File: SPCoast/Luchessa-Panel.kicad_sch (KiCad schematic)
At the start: 21 parts, among them SW8784 783, SW8796 795, SW8800 799, U8004 0x24, U8005 0x25, U8006 0x26

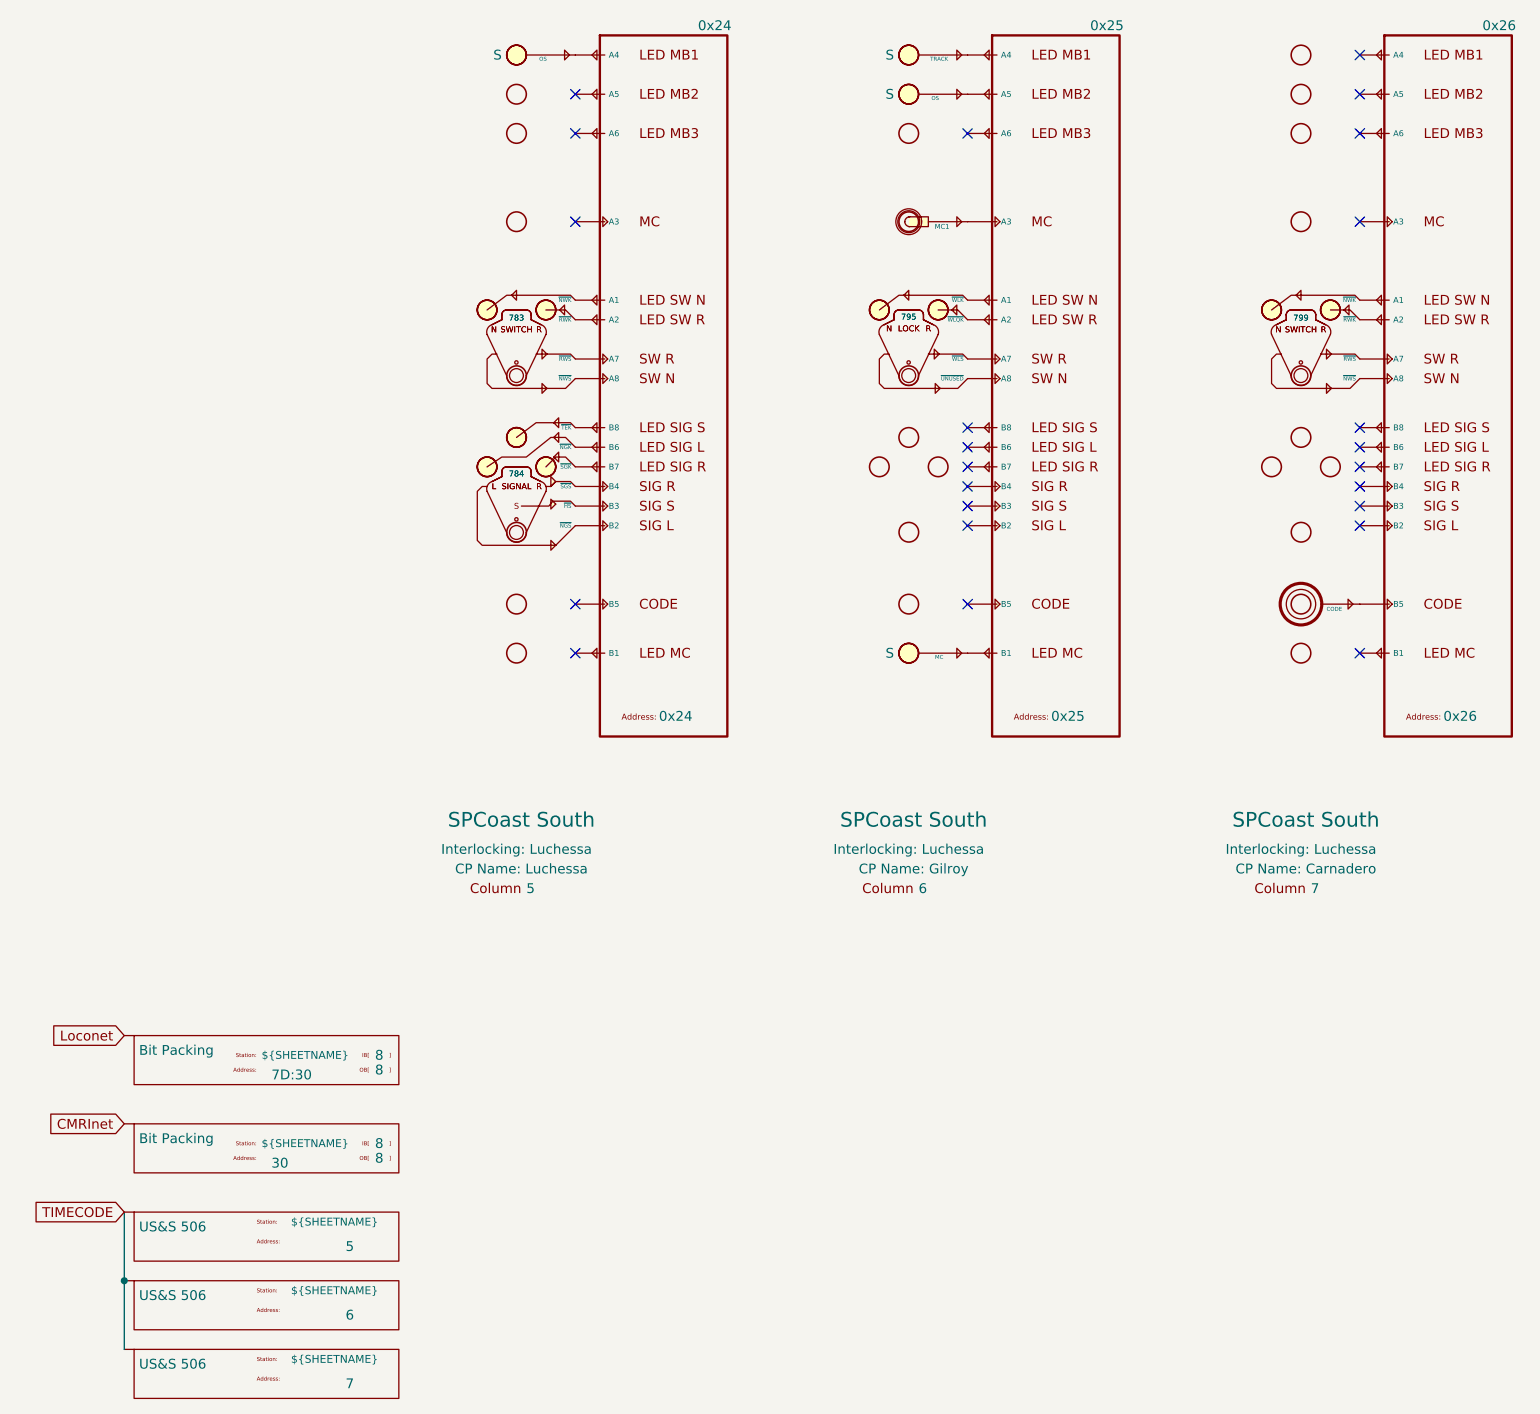
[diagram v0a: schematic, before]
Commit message: refactor(kicad): mast anchors with explicit indication-to-aspect casts; restore fields KiCad reset
Second pass after the cast chains (b4c58d3), decided 2026-10-17: the per-head
anchors Head-CPL/CL/Semaphore were the mast's indication table collapsed into
a symbol. The chain is now

    [Mast 774NAB] -indication- [Cast-Aspect-CPL unit B] -aspect- [Cast-Encoder-CPL] -bits- [chip]

Cast-Aspect-CPL/CL/Semaphore are multi-unit casts, one unit per head letter
(A..E), so placing unit B beside mast 774N is head 774NB with nothing typed;
the reader derives every head name from mast plus unit. Style's home is the
aspect cast. The project ERC now ignores missing_unit and missing_input_pin,
since an aspect cast places only the units its mast has.

CMRI bits: Address is the node (the chip every bit folds into, as for every
other driver), Bit is the bit, UA = ${Address} is a display echo, Value =
UA${Address}.IN.${Bit}.

Restore (SPCoast/edits/2026-10-17-restore-reset-fields.py): the owner's last
KiCad save before 857cae2 ran "update symbols from library" with field reset,
putting library defaults into per-instance fields on nine sheets: every
PanelLamp IndicationToken ("S"), PanelColumn Interlocking ("Luchessa"),
Luchessa encoding Station ("Panel"), Sargent Exp2 PCA9685-PWM 0x27 -> 0x20
(colliding with Exp3), and the 34 Caltrain bit numbers. All 98 values are
restored from the last good netlist export, embedded in the script.

Scripts: SPCoast/edits/2026-10-17-mast-chain.py (second pass; reuses the
first pass's helpers), 2026-10-17-restore-reset-fields.py. __pycache__/
added to .gitignore.

Verified:
- post-restore netlist vs the last good export: no field differs except on
  the anchors the first pass replaced and the intended JMRI blanks
- lint_symbol_fields: 93 symbols, 0 errors (per-unit cast rule)
- kicad-cli ERC: 0 violations; netlist export without warnings
- gate vs post-restore: nets not touching an anchor identical; all 11 aspect
  nets re-sourced from a Cast-Aspect un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
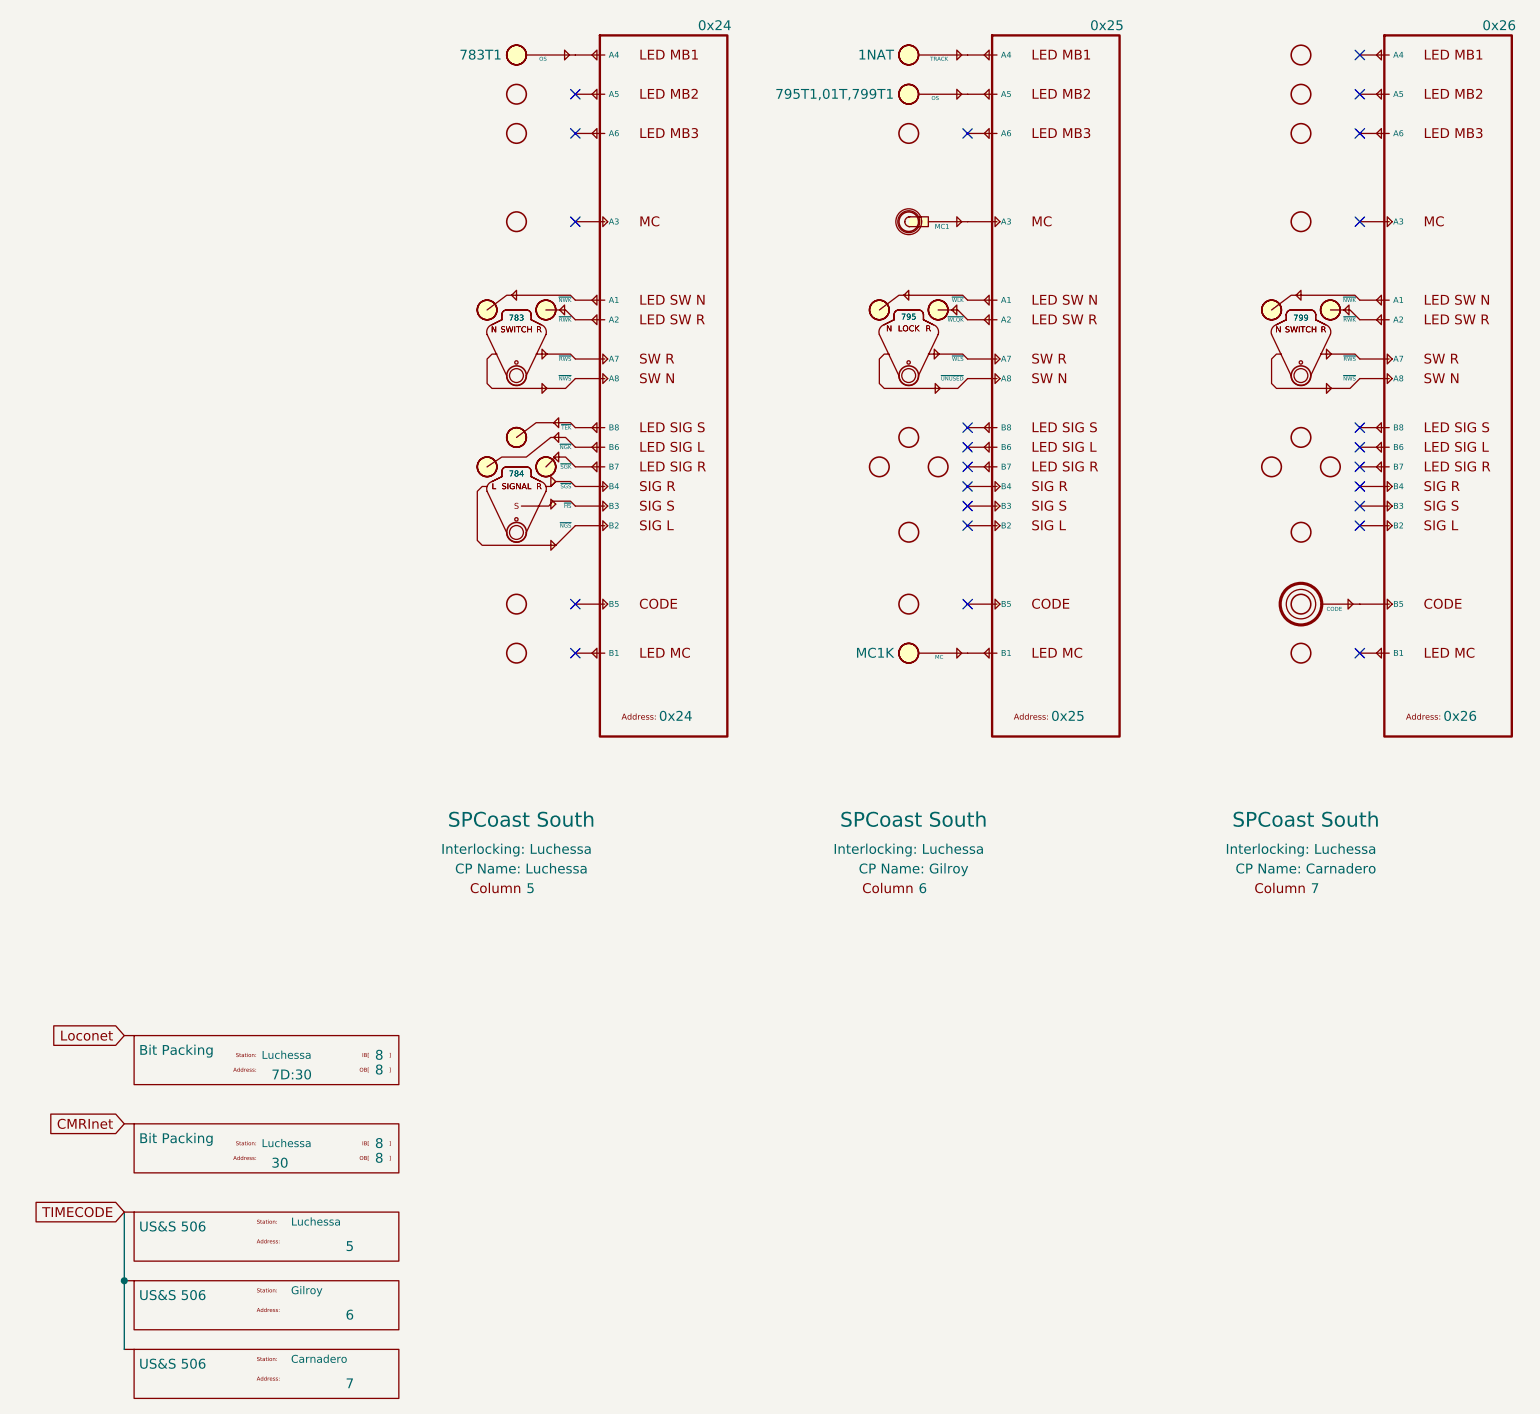
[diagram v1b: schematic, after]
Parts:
- Encoding8002, Encoding8005, Encoding8006: Station ${SHEETNAME} -> Luchessa
- Encoding8003: Station ${SHEETNAME} -> Gilroy
- Encoding8004: Station ${SHEETNAME} -> Carnadero
- LAMP8005: IndicationToken S -> 783T1
- LAMP8006: IndicationToken S -> 1NAT
- LAMP8007: IndicationToken S -> 795T1,01T,799T1
- LAMP8008: IndicationToken S -> MC1K
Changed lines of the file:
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@@
 			)
 		)
-		(property "Station" "${SHEETNAME}"
+		(property "Station" "Gilroy"
 			(at 50.8 186.69 0)
 			(show_name no)
@@
 			)
 		)
-		(property "IndicationToken" "S"
+		(property "IndicationToken" "MC1K"
 			(at 128.905 104.14 0)
 			(show_name no)
@@
 			)
 		)
-		(property "IndicationToken" "S"
+		(property "IndicationToken" "783T1"
 			(at 78.105 26.67 0)
 			(show_name no)
@@
 			)
 		)
-		(property "Station" "${SHEETNAME}"
+		(property "Station" "Luchessa"
 			(at 46.99 167.64 0)
 			(show_name no)
@@
 			)
 		)
-		(property "Station" "${SHEETNAME}"
+		(property "Station" "Luchessa"
 			(at 50.8 177.8 0)
 			(show_name no)
@@
 			)
 		)
-		(property "IndicationToken" "S"
+		(property "IndicationToken" "1NAT"
 			(at 128.905 26.67 0)
 			(show_name no)
@@
 			)
 		)
-		(property "IndicationToken" "S"
+		(property "IndicationToken" "795T1,01T,799T1"
 			(at 128.905 31.75 0)
 			(show_name no)
@@
 			)
 		)
-		(property "Station" "${SHEETNAME}"
+		(property "Station" "Carnadero"
 			(at 50.8 195.58 0)
 			(show_name no)
@@
 			)
 		)
-		(property "Station" "${SHEETNAME}"
+		(property "Station" "Luchessa"
 			(at 46.99 156.21 0)
 			(show_name no)
